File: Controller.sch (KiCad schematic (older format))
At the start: 22 parts, among them CON401 AVR_ISP, J401 Power, J402 Power, J403 Power, J404 Port D, J405 Port B, J406 Port C, J407 ADC6, J408 ADC7, U401 ATMEGA88A-AU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

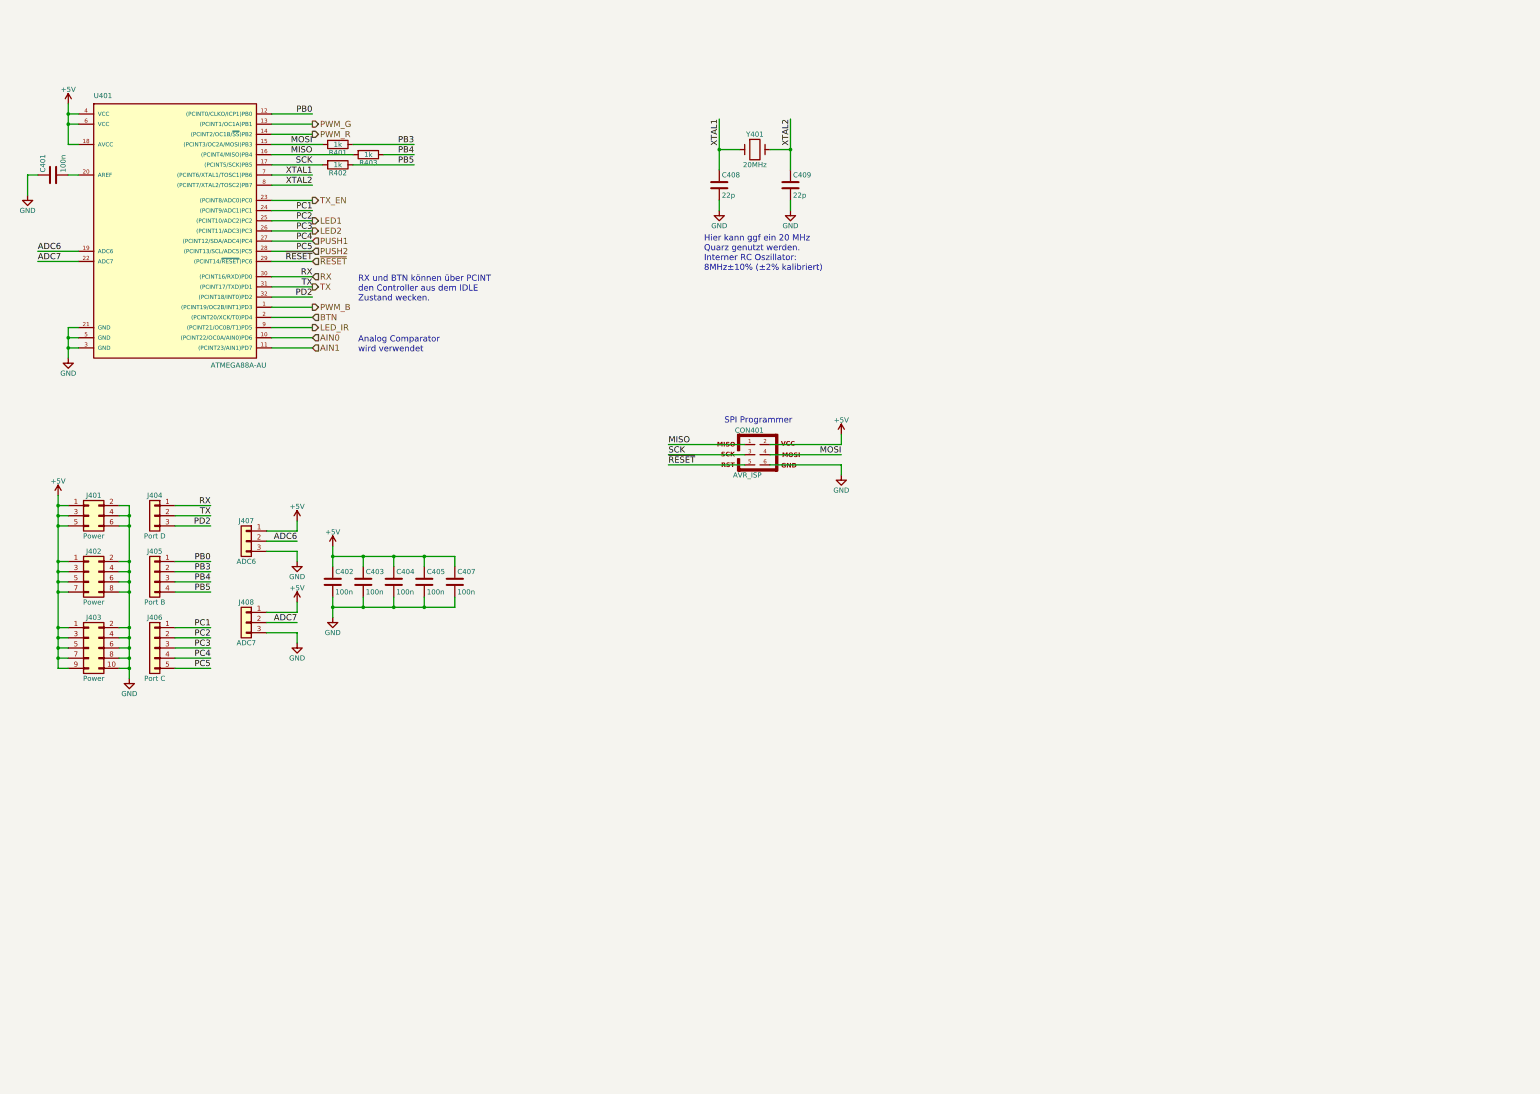
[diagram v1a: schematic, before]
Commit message: ATmega2560 inserted
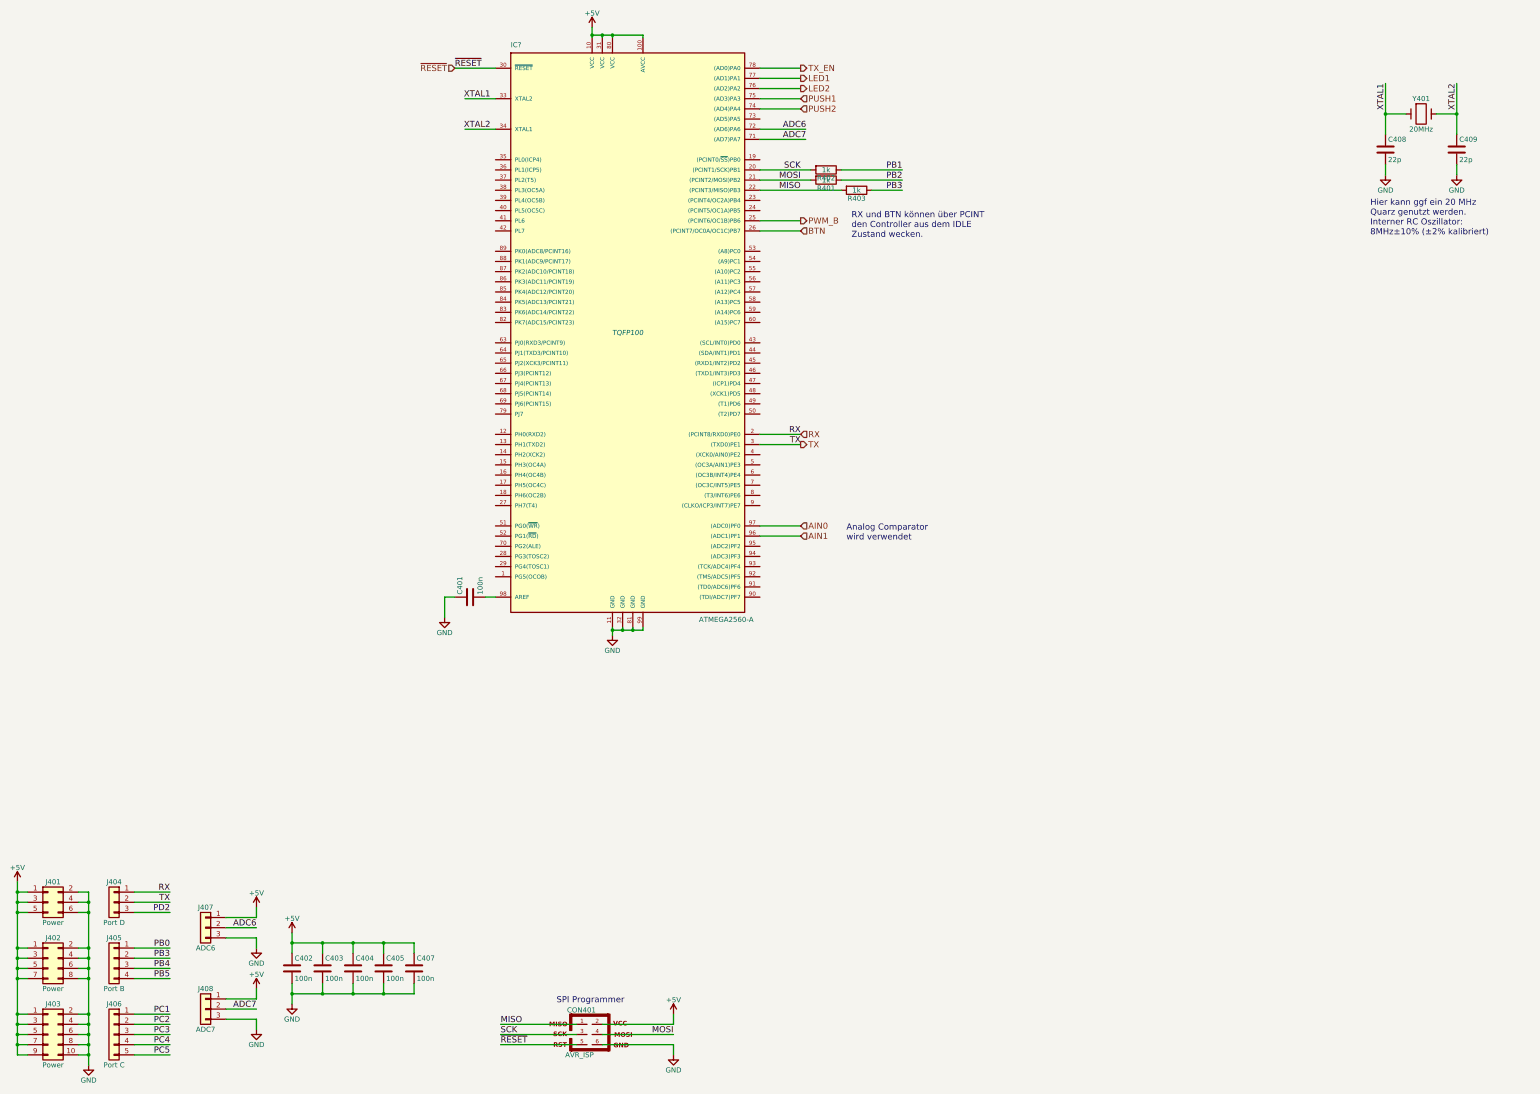
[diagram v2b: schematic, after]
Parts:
- removed U401: ATMEGA88A-AU, Housings_QFP:TQFP-32_7x7mm_Pitch0.8mm, symbol ATMEGA88A-AU
- added IC?: ATMEGA2560-A, TQFP100, symbol ATMEGA2560-A
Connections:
- net +5V: now also IC?.10 (VCC), IC?.100 (AVCC), IC?.31 (VCC), IC?.80 (VCC)
- net ADC6: now also IC?.72 ((AD6)PA6)
- net ADC7: now also IC?.71 ((AD7)PA7)
- net AIN0: now also IC?.97 ((ADC0)PF0)
- net AIN1: now also IC?.96 ((ADC1)PF1)
- net BTN: now also IC?.26 ((PCINT7/OC0A/OC1C)PB7)
- net GND: now also IC?.11 (GND), IC?.32 (GND), IC?.81 (GND), IC?.99 (GND)
- net LED1: now also IC?.77 ((AD1)PA1); no longer J406.2 (Pin_2)
- net LED2: now also IC?.76 ((AD2)PA2); no longer J406.3 (Pin_3)
- net MISO: now also IC?.22 ((PCINT3/MISO)PB3)
- net MOSI: now also IC?.21 ((PCINT2/MOSI)PB2)
- net PB3: now also R403.1; no longer R401.1
- net PB4: no longer R403.1
- net PB5: no longer R402.1
- net PUSH1: now also IC?.75 ((AD3)PA3); no longer J406.4 (Pin_4)
- net PUSH2: now also IC?.74 ((AD4)PA4); no longer J406.5 (Pin_5)
- net PWM_B: now also IC?.25 ((PCINT6/OC1B)PB6)
- net RX: now also IC?.2 ((PCINT8/RXD0)PE0)
- net SCK: now also IC?.20 ((PCINT1/SCK)PB1)
- net TX: now also IC?.3 ((TXD0)PE1)
- net TX_EN: now also IC?.78 ((AD0)PA0)
- net XTAL1: now also IC?.33 (XTAL2)
- net XTAL2: now also IC?.34 (XTAL1)
- net ~RESET: now also IC?.30 (~RESET)
- net at C401.2: now also IC?.98 (AREF)
- new net PB1: R402.1
- new net PB2: R401.1
- new net PC2: J406.2 (Pin_2)
- new net PC3: J406.3 (Pin_3)
- new net PC4: J406.4 (Pin_4)
- new net PC5: J406.5 (Pin_5)
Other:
- moved on the sheet: C401, C402, C403, C404, C405, C407, C408, C409, CON401, J401, J402, J403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
